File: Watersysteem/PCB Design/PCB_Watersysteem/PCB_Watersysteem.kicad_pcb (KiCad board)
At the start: 2 copper layers, 98 parts, among them J1 12V ingang, J10 LED Water Level, J11 LED Nutrient Level, J12 Height Nutrients, J13 Height Mixer, J14 Pomp1, J15 Pomp2, J16 Pomp3, J17 Pomp4, J18 Luchtpomp, J19 Mixer, J2 TTL Connector, J20 UV, J22 230V, J23 ReferentieProbe, J24 Voedingsstoffen 1, J25 Voedingsstoffen 2, J26 Voedingsstoffen 3, J6 Height Water, J7 Endstop Lade0, J8 Endstop Lade1, J9 Endstop UV, K1 AHQSS105DM2FA0G, K2 AHQSS105DM2FA0G, K3 AHQSS105DM2FA0G, K6 AHQSS105DM2FA0G, K7 AHQSS105DM2FA0G, K8 AHQSS105DM2FA0G, K9 AHQSS105DM2FA0G, Q1 BSS138, Q2 BSS138, Q3 BSS138, Q4 BSS138, Q5 BSS138, Q6 BSS138, Q7 BSS138, SW1 EN, SW2 BOOT, U1 ESP32-WROOM-32D, U2 MP1584_Module, U3 AMS1117-3.3, U4 ADS1115IDGS, U5 MCP23017_SO

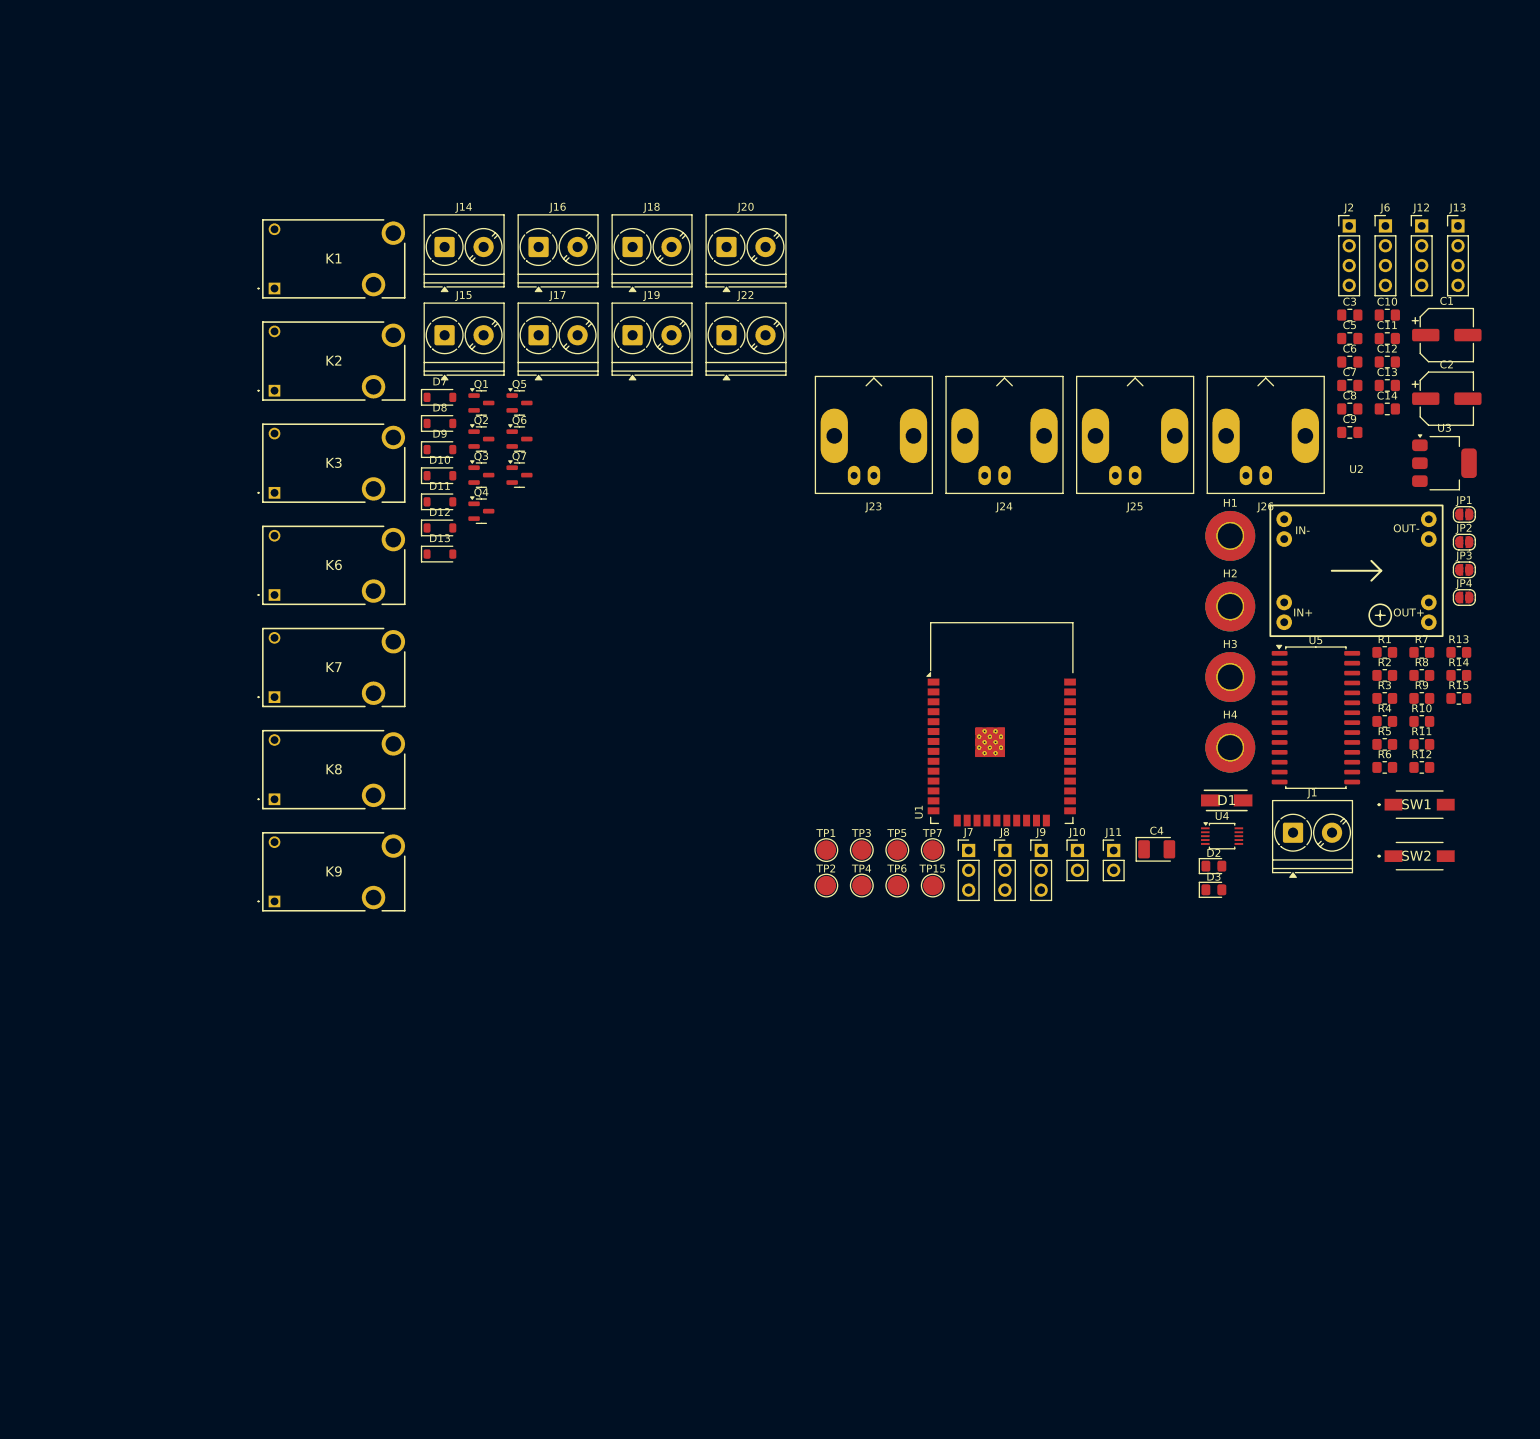
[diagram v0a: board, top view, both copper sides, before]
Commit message: componenten gegroepeerd
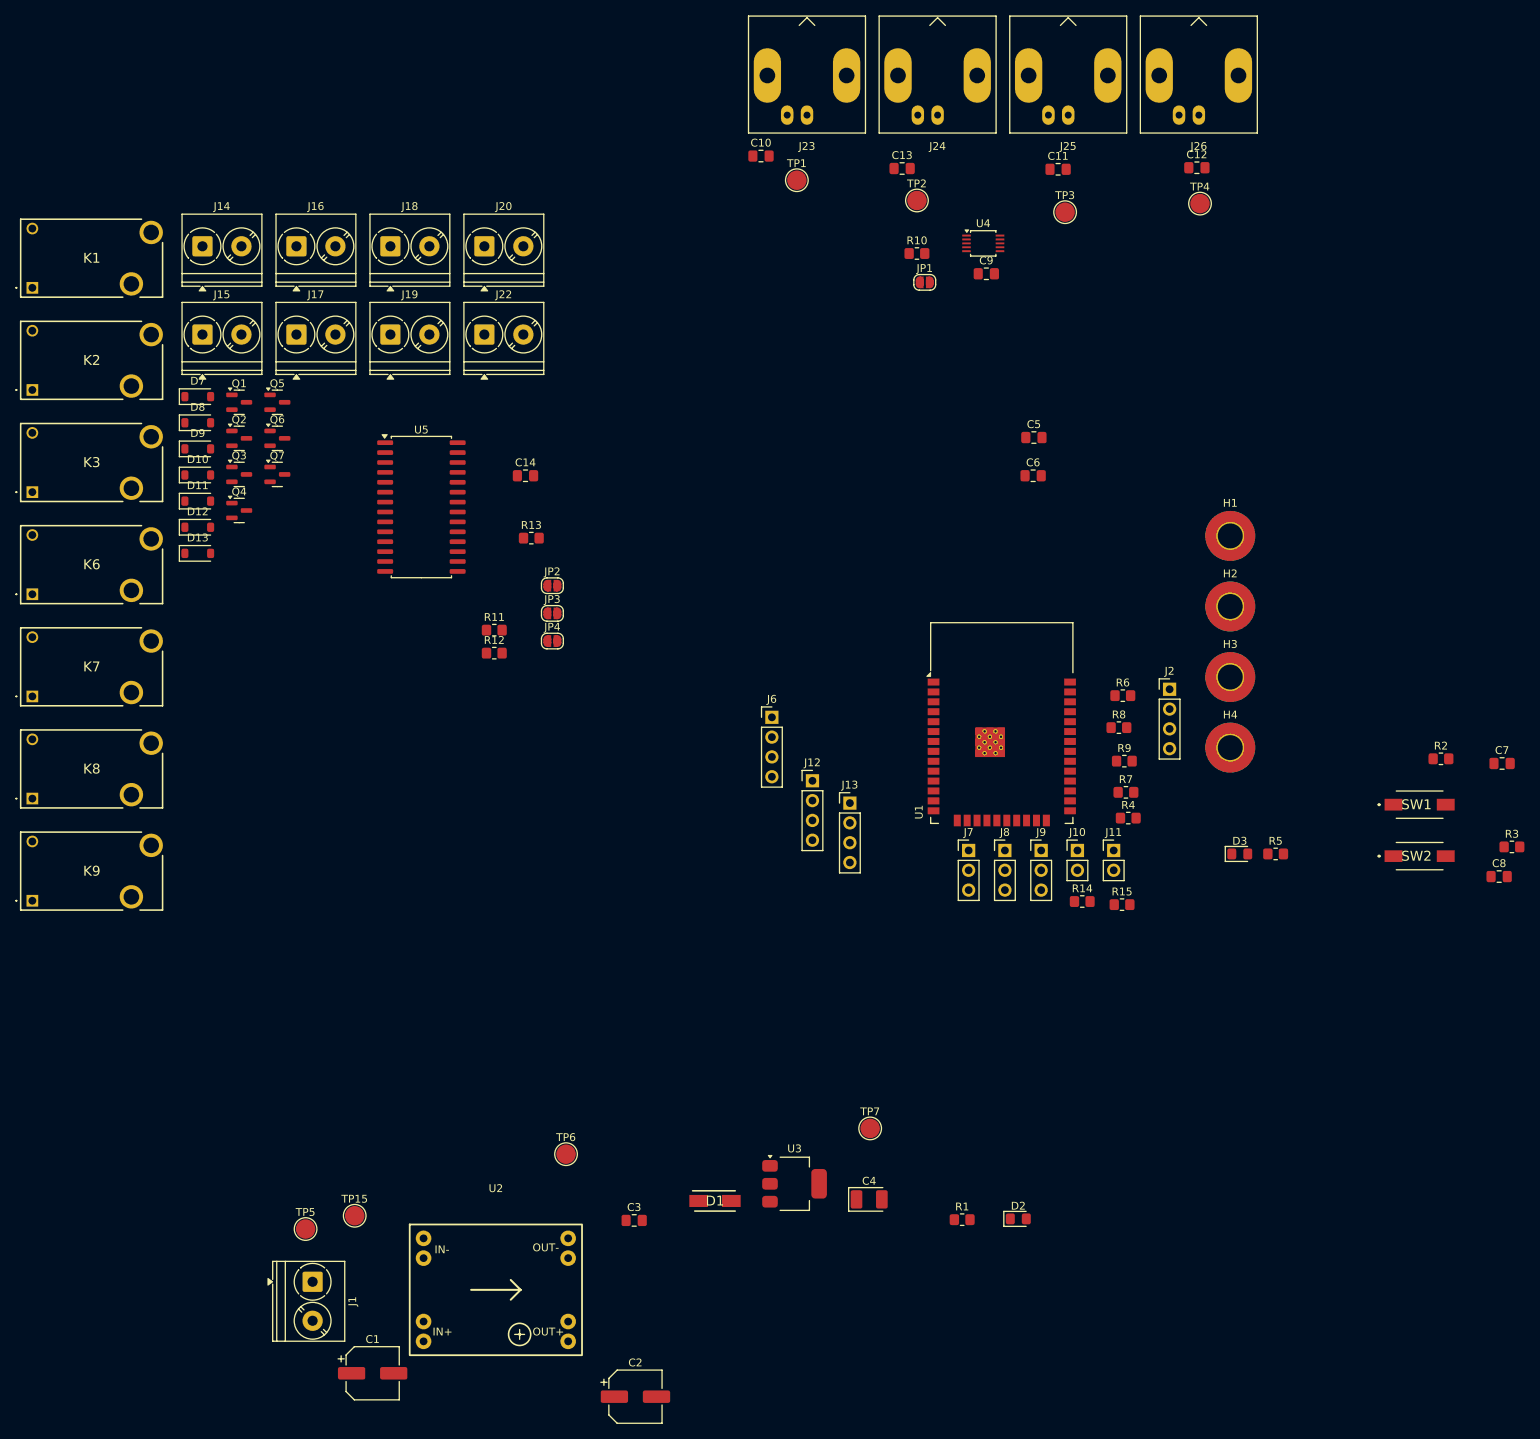
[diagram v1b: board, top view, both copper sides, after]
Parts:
- moved C1 191.6 mm to (69.6, 194.5)
- moved C2 164.9 mm to (103.3, 197.5)
- moved C3 148.0 mm to (103.1, 174.9)
- moved U2 143.8 mm to (85.4, 183.8)
- moved J1 138.3 mm to (61.9, 182.8), turned to -90 degrees
- moved U3 124.4 mm to (123.7, 170.2)
- moved R11 119.8 mm to (85.2, 99.2)
- moved R12 119.8 mm to (85.2, 102.2)
- moved R13 119.8 mm to (90.0, 87.4)
- moved U5 117.8 mm to (75.8, 83.4)
- moved JP2 117.1 mm to (92.7, 93.5)
- moved JP3 117.1 mm to (92.7, 97.0)
- moved JP4 117.1 mm to (92.7, 100.6)
- moved C14 110.9 mm to (89.2, 79.4)
- moved J13 107.5 mm to (130.8, 121.4)
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
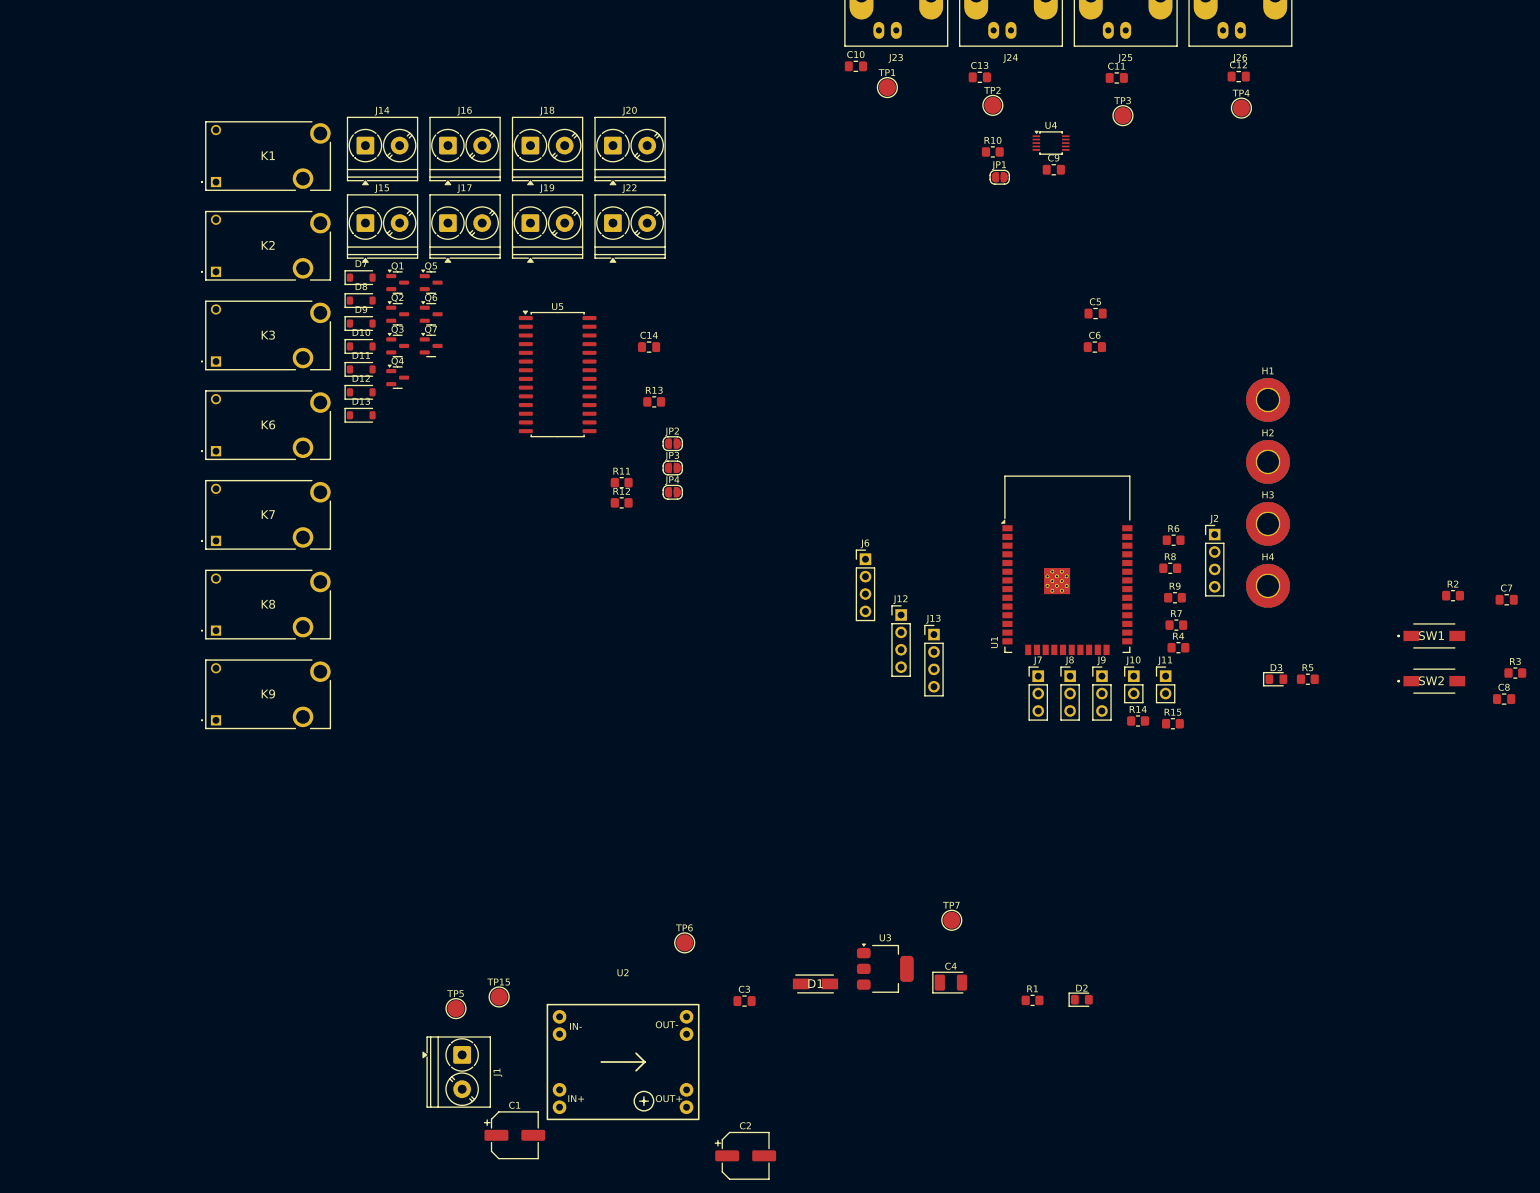
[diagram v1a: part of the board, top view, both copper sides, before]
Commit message: componenten gegroepeerd
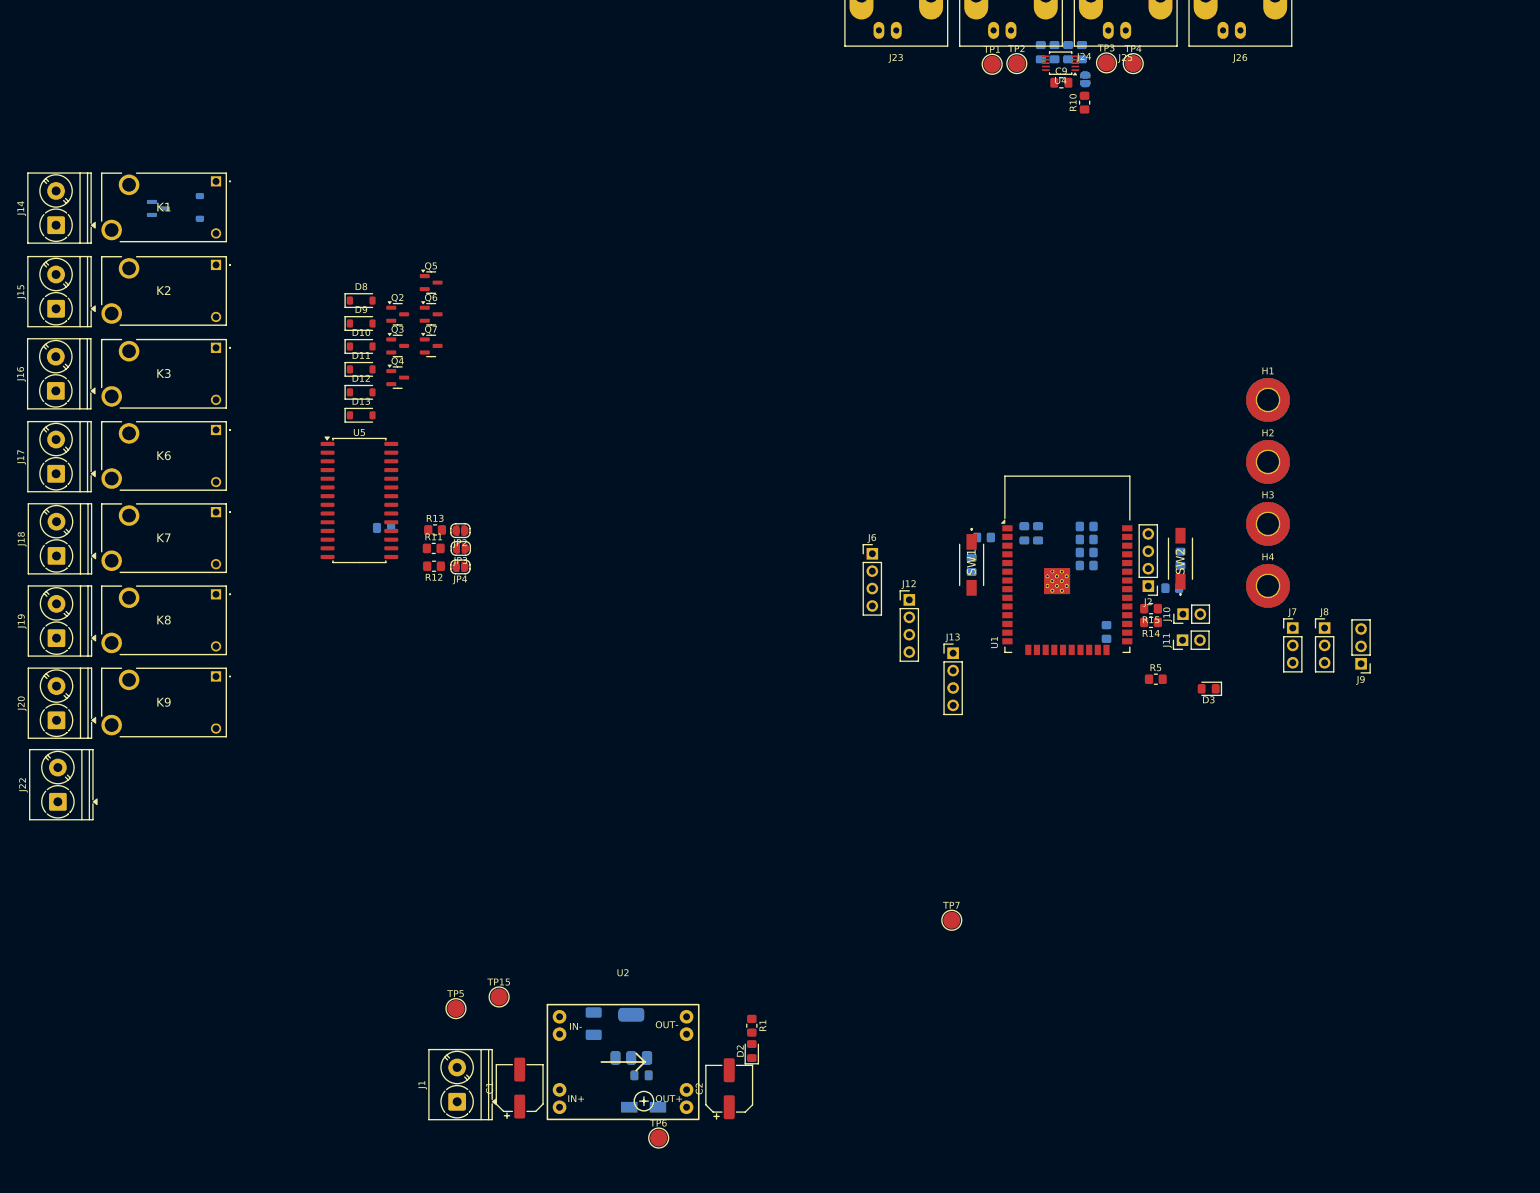
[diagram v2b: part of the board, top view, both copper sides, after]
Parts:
- C10, C11, C12, C13, C14, C3, C4, C5, C6, C7, C8, D1, D7, JP1, Q1, R2, R3, R4, R6, R7, R8, R9, U3: moved to B.Cu
- moved J22 117.1 mm to (2.87, 145.8), turned to 90 degrees
- moved J20 116.8 mm to (2.67, 133.9), turned to 90 degrees
- moved J19 92.0 mm to (2.67, 121.9), turned to 90 degrees
- moved J18 91.5 mm to (2.67, 109.9), turned to 90 degrees
- moved C7 78.3 mm to (136.3, 111.2), turned to -90 degrees
- moved R2 69.0 mm to (138.1, 107.2)
- moved SW1 68.4 mm to (136.3, 111.2), turned to -90 degrees
- moved J17 67.9 mm to (2.60, 97.9), turned to 90 degrees
- moved J16 67.5 mm to (2.57, 85.8), turned to 90 degrees
- moved C4 52.5 mm to (81.1, 178.2), turned to -90 degrees
- moved R3 51.6 mm to (165.6, 114.6), turned to 180 degrees
- moved C8 51.5 mm to (166.8, 110.3), turned to 90 degrees
- moved D2 48.8 mm to (104.2, 182.2), turned to 90 degrees
- moved J15 46.9 mm to (2.60, 73.8), turned to 90 degrees
- moved C14 46.8 mm to (50.5, 105.8), turned to 180 degrees
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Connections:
- U4 pad 1: GND -> Net-(JP1-B)

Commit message: Indeling gemaakt
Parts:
- D10, D11, D12, D13, D8, D9, JP2, JP3, JP4, Q2, Q3, Q4, Q5, Q6, Q7, R11, R12, R13: moved to B.Cu
- moved TP6 200.8 mm to (13.5, 9.50)
- moved TP7 197.4 mm to (2.50, 15.4)
- moved H1 185.0 mm to (2.50, 33.5)
- moved H2 183.6 mm to (2.30, 144.1)
- moved TP15 173.5 mm to (6.00, 12.0)
- moved TP5 173.3 mm to (-4.00, 15.4)
- moved D2 164.2 mm to (39.0, 31.5)
- moved R1 162.7 mm to (36.5, 30.5), turned to 90 degrees
- moved J26 157.9 mm to (60.5, 141.2), turned to -90 degrees
- moved C1 153.7 mm to (10.5, 46.0)
- moved U2 153.4 mm to (25.8, 42.4)
- moved J1 153.4 mm to (1.00, 48.5)
- moved C3 152.6 mm to (23.5, 47.5), turned to 90 degrees
- moved D1 150.5 mm to (30.5, 51.5)
- moved C2 149.3 mm to (32.5, 55.0), turned to 0 degrees
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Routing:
- net 5V: track 0.00 -> 141.8 mm, vias 0 -> 1
- net 12V: track 0.00 -> 75.9 mm
- net 230V: track 0.00 -> 13.2 mm
- net MIXER: track 0.00 -> 10.9 mm
- net AIR: track 0.00 -> 10.5 mm
- net UV: track 0.00 -> 10.2 mm
- net PUMP4: track 0.00 -> 10.1 mm
- net PUMP3: track 0.00 -> 9.68 mm
- net PUMP2: track 0.00 -> 9.27 mm
- net PUMP1: track 0.00 -> 8.87 mm
- net Net-(D1-K): track 0.00 -> 7.12 mm
- net Net-(J20-Pin_2): track 0.00 -> 6.00 mm
- net 3V3: track 0.00 -> 5.90 mm
- net Net-(D8-A): track 0.00 -> 2.86 mm
- net Net-(D9-A): track 0.00 -> 2.82 mm
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- added copper zone on B.Cu, net GND
- added copper zone on F.Cu, net GND
